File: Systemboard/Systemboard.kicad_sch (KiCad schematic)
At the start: 7 parts, among them J1 Conn_01x60, J108 Prog BT, U101 ESP32-WROOM-32E

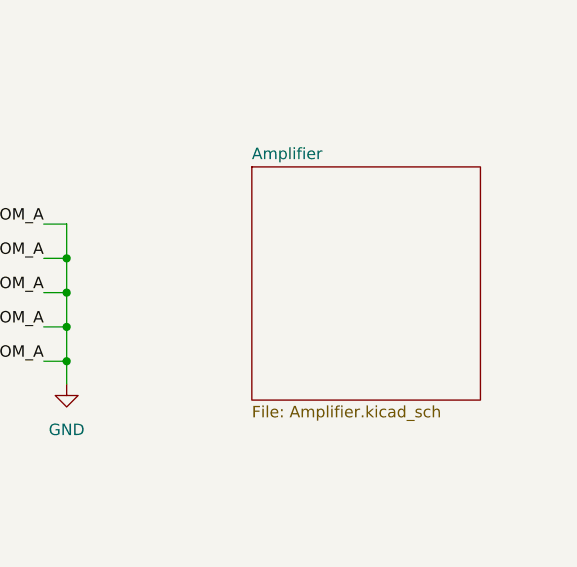
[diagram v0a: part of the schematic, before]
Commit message: Add Amp
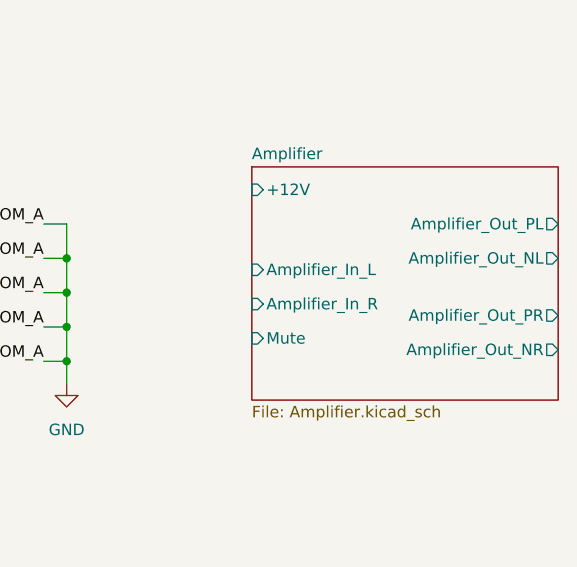
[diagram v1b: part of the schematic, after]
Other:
- sheet Amplifier ports: added +12V, Amplifier_In_L, Amplifier_In_R, Amplifier_Out_NL, Amplifier_Out_NR, Amplifier_Out_PL, Amplifier_Out_PR, Mute; removed none
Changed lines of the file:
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@@
 	(sheet
 		(at 228.854 127)
-		(size 25.4 25.908)
+		(size 34.036 25.908)
 		(exclude_from_sim no)
 		(in_bom yes)
@@
 			)
 		)
+		(pin "Amplifier_Out_PL" output
+			(at 262.89 133.35 0)
+			(effects
+				(font
+					(size 1.27 1.27)
+				)
+				(justify right)
+			)
+		)
+		(pin "Amplifier_Out_PR" output
+			(at 262.89 143.51 0)
+			(effects
+				(font
+					(size 1.27 1.27)
+				)
+				(justify right)
+			)
+		)
+		(pin "Amplifier_Out_NR" output
+			(at 262.89 147.32 0)
+			(effects
+				(font
+					(size 1.27 1.27)
+				)
+				(justify right)
+			)
+		)
+		(pin "Amplifier_Out_NL" output
+			(at 262.89 137.16 0)
+			(effects
+				(font
+					(size 1.27 1.27)
+				)
+				(justify right)
+			)
+		)
+		(pin "Amplifier_In_R" input
+			(at 228.854 142.24 180)
+			(effects
+				(font
+					(size 1.27 1.27)
+				)
+				(justify left)
+			)
+		)
+		(pin "+12V" input
+			(at 228.854 129.54 180)
+			(effects
+				(font
+					(size 1.27 1.27)
+				)
+				(justify left)
+			)
+		)
+		(pin "Mute" input
+			(at 228.854 146.05 180)
+			(effects
+				(font
+					(size 1.27 1.27)
+				)
+				(justify left)
+			)
+		)
+		(pin "Amplifier_In_L" input
+			(at 228.854 138.43 180)
+			(effects
+				(font
+					(size 1.27 1.27)
+				)
+				(justify left)
+			)
+		)

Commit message: Update Systemboard.kicad_sch
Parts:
- U101: DigiKey Part # (none) -> 5407-ESP32-WROOM-32E-N16CT-ND
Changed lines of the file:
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@@
+			)
+		)
+		(property "DigiKey Part #" "5407-ESP32-WROOM-32E-N16CT-ND"
+			(at 81.28 137.16 0)
+			(effects
+				(font
+					(size 1.27 1.27)
+				)
+				(hide yes)
 			)
 		)

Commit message: add jlc part numbers
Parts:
- C101: JLCPCB Part # (none) -> C23630
- R101, R103: footprint Resistor_SMD:R_0402_1005Metric_Pad0.72x0.64mm_HandSolder -> Resistor_SMD:R_0603_1608Metric_Pad0.98x0.95mm_HandSolder; DigiKey Part # P47DCCT-ND -> 311-47.0HRCT-ND; JLCPCB Part # (none) -> C23182
- R117: JLCPCB Part # (none) -> C25744
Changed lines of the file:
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@@
 			)
 		)
-		(property "Footprint" "Resistor_SMD:R_0402_1005Metric_Pad0.72x0.64mm_HandSolder"
+		(property "Footprint" "Resistor_SMD:R_0603_1608Metric_Pad0.98x0.95mm_HandSolder"
 			(at 114.3 104.902 90)
 			(effects
@@
 			)
 		)
-		(property "DigiKey Part #" "P47DCCT-ND"
+		(property "DigiKey Part #" "311-47.0HRCT-ND"
+			(at 114.3 106.68 90)
+			(effects
+				(font
+					(size 1.27 1.27)
+				)
+				(hide yes)
+			)
+		)
+		(property "JLCPCB Part #" "C23182"
 			(at 114.3 106.68 90)
 			(effects
@@
 			)
 		)
+		(property "JLCPCB Part #" "C23630"
+			(at 160.02 41.91 0)
+			(effects
+				(font
+					(size 1.27 1.27)
+				)
+				(hide yes)
+			)
+		)
 		(pin "2"
 		)
@@
 		)
 		(property "DigiKey Part #" "1276-3431-1-ND"
+			(at 160.02 31.75 0)
+			(effects
+				(font
+					(size 1.27 1.27)
+				)
+				(hide yes)
+			)
+		)
+		(property "JLCPCB Part #" "C25744"
 			(at 160.02 31.75 0)
 			(effects
@@
 			)
 		)
-		(property "Footprint" "Resistor_SMD:R_0402_1005Metric_Pad0.72x0.64mm_HandSolder"
+		(property "Footprint" "Resistor_SMD:R_0603_1608Metric_Pad0.98x0.95mm_HandSolder"
 			(at 171.45 35.052 90)
 			(effects
@@
 			)
 		)
-		(property "DigiKey Part #" "P47DCCT-ND"
+		(property "DigiKey Part #" "311-47.0HRCT-ND"
+			(at 171.45 36.83 90)
+			(effects
+				(font
+					(size 1.27 1.27)
+				)
+				(hide yes)
+			)
+		)
+		(property "JLCPCB Part #" "C23182"
 			(at 171.45 36.83 90)
 			(effects
@@
 			)
 		)
+		(property "JLCPCB Part #" ""
+			(at 116.84 35.56 0)
+			(effects
+				(font
+					(size 1.27 1.27)
+				)
+				(hide yes)
+			)
+		)
 		(pin "1"
 		)
@@
 			)
 		)
+		(property "JLCPCB Part #" ""
+			(at 26.67 100.33 0)
+			(effects
+				(font
+					(size 1.27 1.27)
+				)
+				(hide yes)
+			)
+		)
 		(pin "17"
 		)
@@
 			(at 81.28 137.16 0)
 			(effects
+				(font
+					(size 1.27 1.27)
+				)
+				(hide yes)
+			)
+		)
+		(property "JLCPCB Part #" ""
+			(at 81.28 137.16 0)
+			(effects

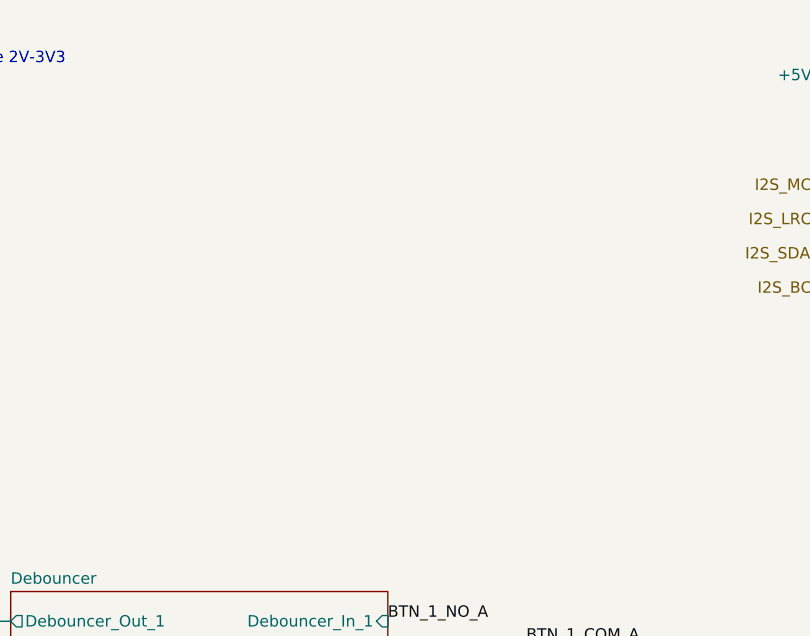
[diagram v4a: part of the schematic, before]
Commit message: user save usb dac port
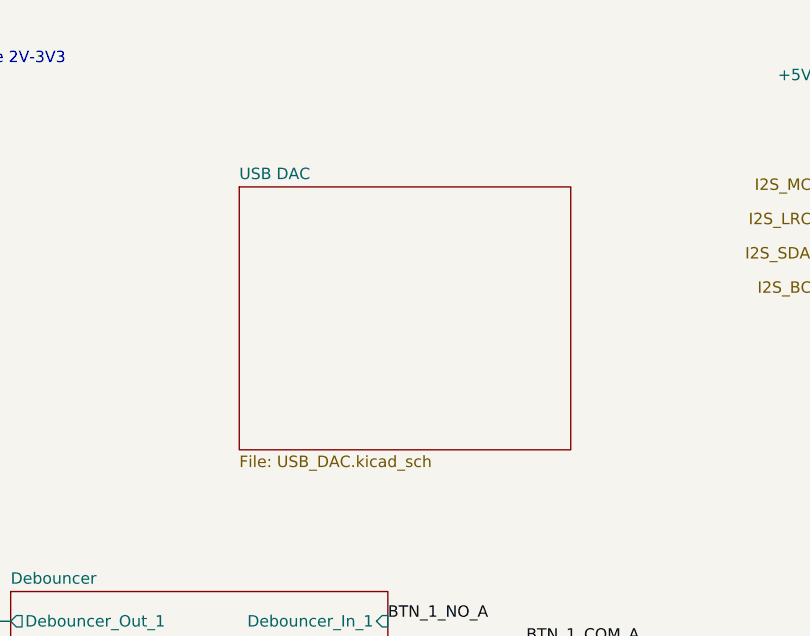
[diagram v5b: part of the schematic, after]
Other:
- added sheet USB DAC (USB_DAC.kicad_sch)
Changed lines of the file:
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@@
+		)
+	)
+	(sheet
+		(at 161.29 82.55)
+		(size 36.83 29.21)
+		(exclude_from_sim no)
+		(in_bom yes)
+		(on_board yes)
+		(dnp no)
+		(fields_autoplaced yes)
+		(stroke
+			(width 0.1524)
+			(type solid)
+		)
+		(fill
+			(color 0 0 0 0)
+		)
+		(property "Sheetname" "USB DAC"
+			(at 161.29 81.8384 0)
+			(show_name no)
+			(do_not_autoplace no)
+			(effects
+				(font
+					(size 1.27 1.27)
+				)
+				(justify left bottom)
+			)
+		)
+		(property "Sheetfile" "USB_DAC.kicad_sch"
+			(at 161.29 112.3446 0)
+			(show_name no)
+			(do_not_autoplace no)
+			(effects
+				(font
+					(size 1.27 1.27)
+				)
+				(justify left top)
+			)
+		)
+		(instances
+			(project "Systemboard"
+				(path "/2f4830bd-672b-4d5b-b8d7-989ae91c893c"
+					(page "6")
+				)
+			)
 		)
 	)

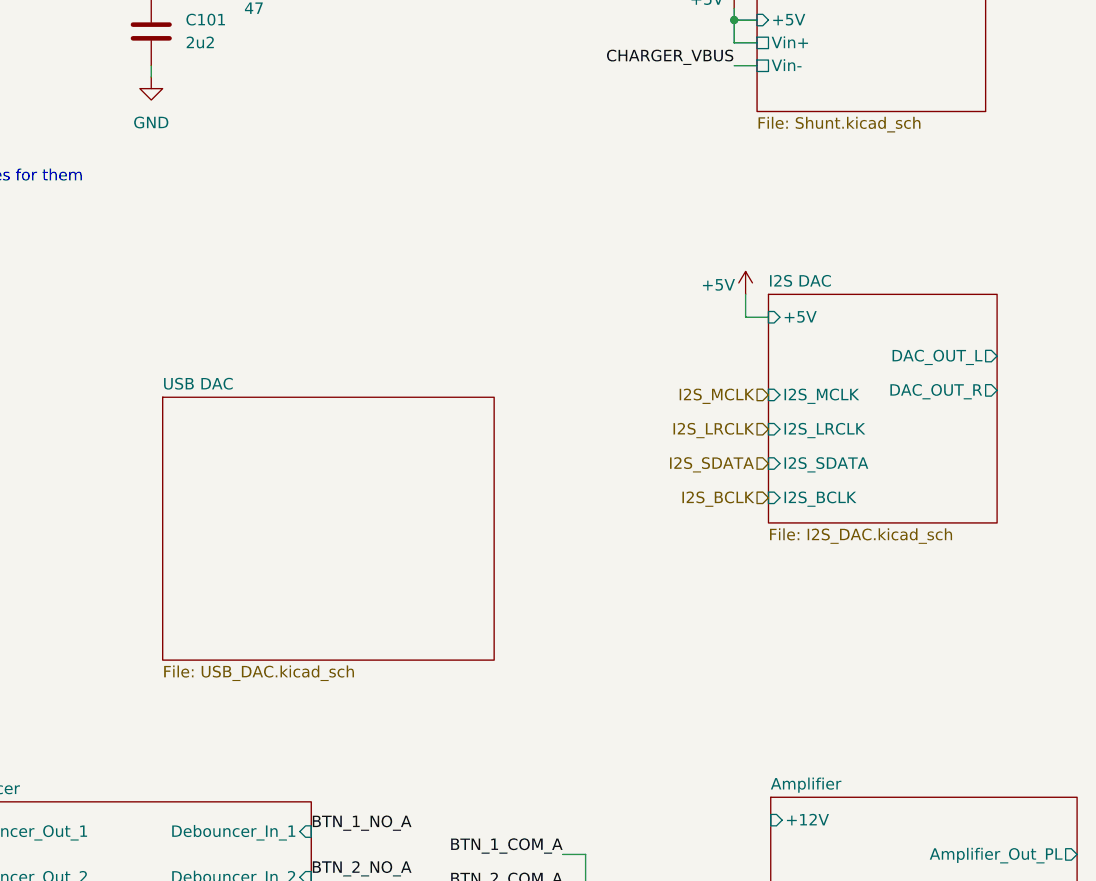
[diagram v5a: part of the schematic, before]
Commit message: port usb dac
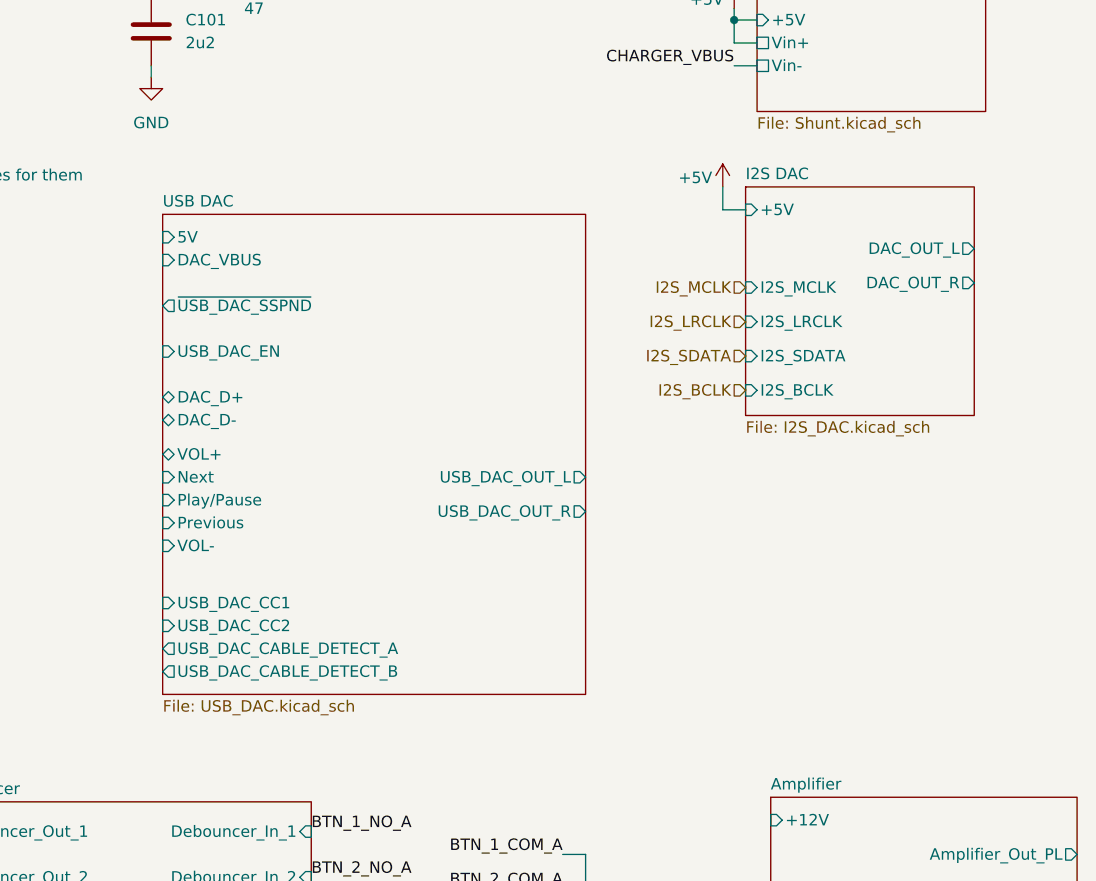
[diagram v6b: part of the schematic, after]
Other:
- sheet USB DAC ports: added 5V, DAC_D+, DAC_D-, DAC_VBUS, Next, Play/Pause, Previous, USB_DAC_CABLE_DETECT_A, USB_DAC_CABLE_DETECT_B, USB_DAC_CC1, USB_DAC_CC2, USB_DAC_EN, USB_DAC_OUT_L, USB_DAC_OUT_R, VOL+, VOL-, ~{USB_DAC_SSPND}; removed none
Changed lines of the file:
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@@
 	(wire
 		(pts
-			(xy 226.06 71.12) (xy 226.06 73.66)
+			(xy 223.52 59.182) (xy 223.52 61.722)
 		)
 		(stroke
@@
 	(wire
 		(pts
-			(xy 226.06 73.66) (xy 228.6 73.66)
+			(xy 223.52 61.722) (xy 226.06 61.722)
 		)
 		(stroke
@@
 	(hierarchical_label "I2S_MCLK"
 		(shape input)
-		(at 228.6 82.296 180)
+		(at 226.06 70.358 180)
 		(effects
 			(font
@@
 	(hierarchical_label "I2S_SDATA"
 		(shape input)
-		(at 228.6 89.916 180)
+		(at 226.06 77.978 180)
 		(effects
 			(font
@@
 	(hierarchical_label "I2S_BCLK"
 		(shape input)
-		(at 228.6 93.726 180)
+		(at 226.06 81.788 180)
 		(effects
 			(font
@@
 	(hierarchical_label "I2S_LRCLK"
 		(shape input)
-		(at 228.6 86.106 180)
+		(at 226.06 74.168 180)
 		(effects
 			(font
@@
 	(symbol
 		(lib_id "power:+5V")
-		(at 226.06 71.12 0)
+		(at 223.52 59.182 0)
 		(unit 1)
 		(body_style 1)
@@
 		(dnp no)
 		(property "Reference" "#PWR0121"
-			(at 226.06 74.93 0)
+			(at 223.52 62.992 0)
 			(hide yes)
 			(show_name no)
@@
 		)
 		(property "Value" "+5V"
-			(at 223.012 70.104 0)
+			(at 220.472 58.166 0)
 			(show_name no)
 			(do_not_autoplace no)
@@
 		)
 		(property "Footprint" ""
-			(at 226.06 71.12 0)
+			(at 223.52 59.182 0)
 			(hide yes)
 			(show_name no)
@@
 		)
 		(property "Datasheet" ""
-			(at 226.06 71.12 0)
+			(at 223.52 59.182 0)
 			(hide yes)
 			(show_name no)
@@
 		)
 		(property "Description" "Power symbol creates a global label with name \"+5V\""
-			(at 226.06 71.12 0)
+			(at 223.52 59.182 0)
 			(hide yes)
 			(show_name no)
@@
 	)
 	(sheet
-		(at 228.6 71.12)
+		(at 226.06 59.182)
 		(size 25.4 25.4)
 		(exclude_from_sim no)
@@
 		)
 		(property "Sheetname" "I2S DAC"
-			(at 228.6 70.4084 0)
+			(at 226.06 58.4704 0)
 			(show_name no)
 			(do_not_autoplace no)
@@
 		)
 		(property "Sheetfile" "I2S_DAC.kicad_sch"
-			(at 228.6 97.1046 0)
+			(at 226.06 85.1666 0)
 			(show_name no)
 			(do_not_autoplace no)
@@
 		)
 		(pin "+5V" input
-			(at 228.6 73.66 180)
+			(at 226.06 61.722 180)
 			(effects
 				(font
@@
 		)
 		(pin "I2S_BCLK" input
-			(at 228.6 93.726 180)
+			(at 226.06 81.788 180)
 			(effects
 				(font
@@
 		)
 		(pin "I2S_LRCLK" input
-			(at 228.6 86.106 180)
+			(at 226.06 74.168 180)
 			(effects
 				(font
@@
 		)
 		(pin "I2S_SDATA" input
-			(at 228.6 89.916 180)
+			(at 226.06 77.978 180)
 			(effects
 				(font
@@
 		)
 		(pin "DAC_OUT_L" output
-			(at 254 77.978 0)
+			(at 251.46 66.04 0)
 			(effects
 				(font
@@
 		)
 		(pin "DAC_OUT_R" output
-			(at 254 81.788 0)
+			(at 251.46 69.85 0)
 			(effects
 				(font
@@
 		)
 		(pin "I2S_MCLK" input
-			(at 228.6 82.296 180)
+			(at 226.06 70.358 180)
 			(effects
 				(font
@@
 	)
 	(sheet
-		(at 161.29 82.55)
-		(size 36.83 29.21)
+		(at 161.29 62.23)
+		(size 46.99 53.34)
 		(exclude_from_sim no)
 		(in_bom yes)
@@
 		)
 		(property "Sheetname" "USB DAC"
-			(at 161.29 81.8384 0)
+			(at 161.29 61.5184 0)
 			(show_name no)
 			(do_not_autoplace no)
@@
 		)
 		(property "Sheetfile" "USB_DAC.kicad_sch"
-			(at 161.29 112.3446 0)
+			(at 161.29 116.1546 0)
 			(show_name no)
 			(do_not_autoplace no)
@@
 			)
 		)
+		(pin "5V" input
+			(at 161.29 64.77 180)
+			(effects
+				(font
+					(size 1.27 1.27)
+				)
+				(justify left)
+			)
+		)
+		(pin "USB_DAC_EN" input
+			(at 161.29 77.47 180)
+			(effects
+				(font
+					(size 1.27 1.27)
+				)
+				(justify left)
+			)
+		)
+		(pin "Play{slash}Pause" input
+			(at 161.29 93.98 180)
+			(effects
+				(font
+					(size 1.27 1.27)
+				)
+				(justify left)
+			)
+		)
+		(pin "USB_DAC_CC2" input
+			(at 161.29 107.95 180)
+			(effects
+				(font
+					(size 1.27 1.27)
+				)
+				(justify left)
+			)
+		)
+		(pin "USB_DAC_CABLE_DETECT_A" output
+			(at 161.29 110.49 180)
+			(effects
+				(font
+					(size 1.27 1.27)
+				)
+				(justify left)
+			)
+		)
+		(pin "~{USB_DAC_SSPND}" output
+			(at 161.29 72.39 180)
+			(effects
+				(font
+					(size 1.27 1.27)
+				)
+				(justify left)
+			)
+		)
+		(pin "USB_DAC_OUT_L" output
+			(at 208.28 91.44 0)
+			(effects
+				(font
+					(size 1.27 1.27)
+				)
+				(justify right)
+			)
+		)
+		(pin "USB_DAC_OUT_R" output
+			(at 208.28 95.25 0)
+			(effects
+				(font
+					(size 1.27 1.27)
+				)
+				(justify right)
+			)
+		)
+		(pin "DAC_D+" bidirectional
+			(at 161.29 82.55 180)
+			(effects
+				(font
+					(size 1.27 1.27)
+				)
+				(justify left)
+			)
+		)
+		(pin "DAC_D-" bidirectional
+			(at 161.29 85.09 180)
+			(effects
+				(font
+					(size 1.27 1.27)
+				)
+				(justify left)
+			)
+		)
+		(pin "VOL-" input
+			(at 161.29 99.06 180)
+			(effects
+				(font
+					(size 1.27 1.27)
+				)
+				(justify left)
+			)
+		)
+		(pin "VOL+" bidirectional
+			(at 161.29 88.9 180)
+			(effects
+				(font
+					(size 1.27 1.27)
+				)
+				(justify left)
+			)
+		)
+		(pin "Next" input
+			(at 161.29 91.44 180)
+			(effects
+				(font
+					(size 1.27 1.27)
+				)
+				(justify left)
+			)
+		)
+		(pin "Previous" input
+			(at 161.29 96.52 180)
+			(effects
+				(font
+					(size 1.27 1.27)
+				)
+				(justify left)
+			)
+		)
+		(pin "USB_DAC_CC1" input
+			(at 161.29 105.41 180)
+			(effects
+				(font
+					(size 1.27 1.27)
+				)
+				(justify left)
+			)
+		)
+		(pin "USB_DAC_CABLE_DETECT_B" output
+			(at 161.29 113.03 180)
+			(effects
+				(font
+					(size 1.27 1.27)
+				)
+				(justify left)
+			)
+		)
+		(pin "DAC_VBUS" input
+			(at 161.29 67.31 180)
+			(effects
+				(font
+					(size 1.27 1.27)
+				)
+				(justify left)
+			)
+		)

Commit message: user save
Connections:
- net BTN_2_COM_B is gone; now on net BTN_1_COM_B: J1.51 (Pin_51)
- net BTN_3_COM_B is gone; now on net BTN_1_COM_B: J1.45 (Pin_45)
- net BTN_4_COM_B is gone; now on net BTN_1_COM_B: J1.39 (Pin_39)
- net BTN_5_COM_B is gone; now on net BTN_1_COM_B: J1.33 (Pin_33)
- net USB_DAC_EN: now reaches U101.16 (IO13)
- net USB_DAC_CABLE_DETECT_A: now reaches U101.31 (IO19)
- net USB_DAC_CABLE_DETECT_B: now reaches U101.33 (IO21)
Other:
- note added: "check whether the headset uses NC or NO switches and reserve that switches for them amplifier power supply high-current 5V, +/-12V maybe, high-current dimmable 2V-3V3 reed switches amp input mux"
- note removed: "check whether the headset uses NC or NO switches and reserve that switches for them amplifier power supply high-current 5V, +/-12V maybe, high-current dimmable 2V-3V3 reed switches"

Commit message: user save
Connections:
- net MUTE: now reaches U101.24 (IO2)
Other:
- added sheet Amplifier Input Mux (Amplifier_Input_Mux.kicad_sch)
- sheet Amplifier ports: added none; removed +12V
- sheet I2S DAC ports: added none; removed +5V
- sheet Shunt ports: added none; removed +5V, Vin+
- sheet USB DAC ports: added none; removed 5V
- moved on the sheet: C101, J108, R101, R117
